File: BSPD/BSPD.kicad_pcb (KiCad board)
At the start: 2 copper layers, 100.3 x 69.5 mm, 81 parts, among them Q1 BC548, Q2 BC548, Q3 BC548, Q4 BC548, Q5 BC548, SW1 SW_DPDT_x2, U1 TL431D, U2 LM358, U3 LM358, U4 ICL7660, U5 LM358, U6 4001

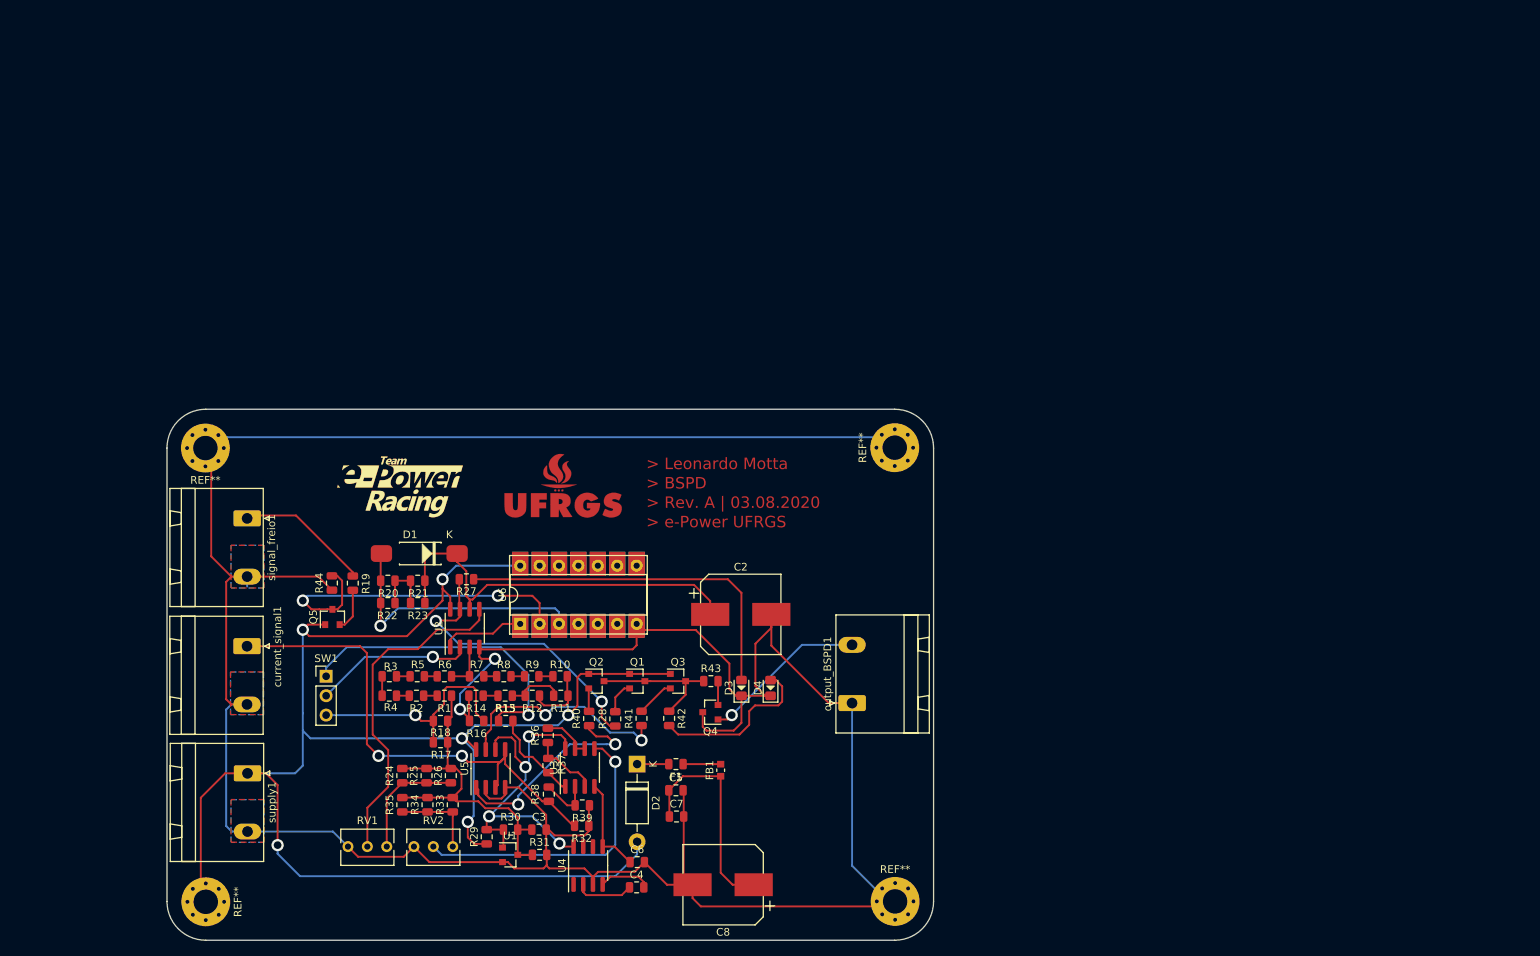
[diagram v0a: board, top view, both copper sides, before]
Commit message: schematic update BSPD and new layout not finishet
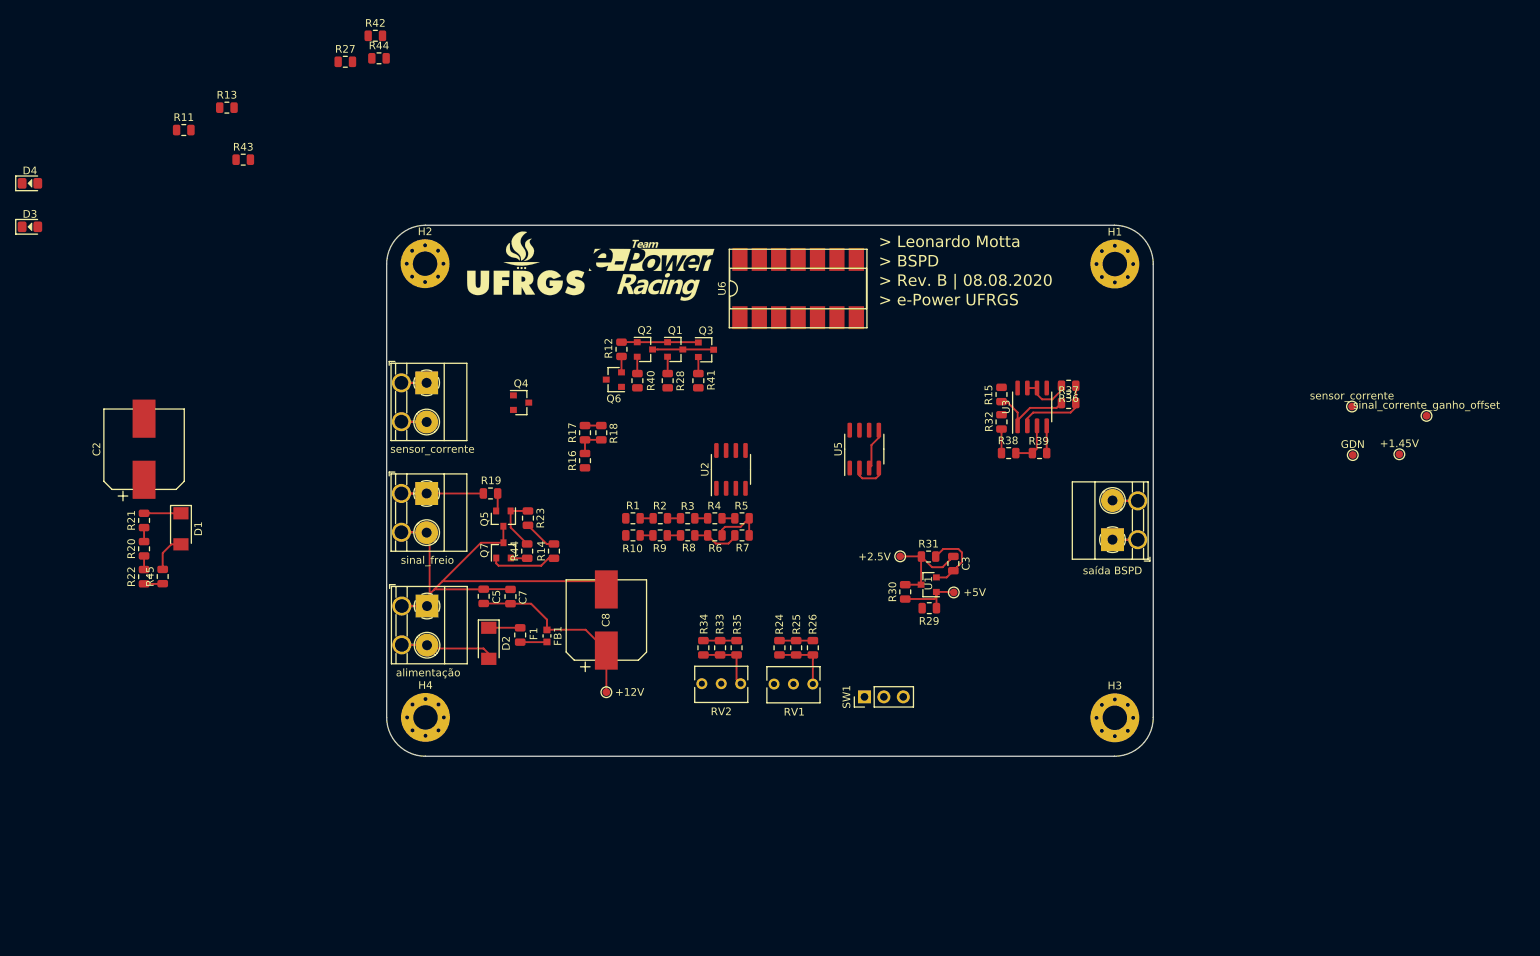
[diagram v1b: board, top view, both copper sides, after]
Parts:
- removed C4: 10uF, Capacitor_SMD:C_0805_2012Metric
- removed C6: 100nF, Capacitor_SMD:C_0805_2012Metric
- removed the R44 at (87.6, 119.4)
- removed REF** (x4): MountingHole_3.2mm_M3_Pad_Via, e-Power:MountingHole_3.2mm_M3_Pad_Via
- removed U4: ICL7660, Package_SO:SOIC-8_3.9x4.9mm_P1.27mm
- removed current_signal1, output_BSPD1, signal_freio1, supply1: Screw_Terminal_01x02, Connector_Phoenix_GMSTB:PhoenixContact_GMSTBA_2,5_2-G-7,62_1x02_P7.62mm_Horizontal
- added H1: MountingHole_Pad, e-Power:MountingHole_3.2mm_M3_Pad_Via, F.Cu at (190.1, 77.6)
- added H2: MountingHole_Pad, e-Power:MountingHole_3.2mm_M3_Pad_Via, F.Cu at (99.8, 77.6)
- added H3: MountingHole_Pad, e-Power:MountingHole_3.2mm_M3_Pad_Via, F.Cu at (190.1, 137.0)
- added H4: MountingHole_Pad, e-Power:MountingHole_3.2mm_M3_Pad_Via, F.Cu at (99.9, 137.0)
- added Q6: BC557, Package_TO_SOT_SMD:SOT-23, F.Cu at (124.5, 92.7)
- added Q7: BC548, Package_TO_SOT_SMD:SOT-23, F.Cu at (110.1, 115.1)
- added R44: 1k, Resistor_SMD:R_0805_2012Metric, F.Cu at (93.8, 50.7)
- added R44: 10k, Resistor_SMD:R_0805_2012Metric, F.Cu at (113.2, 115.2)
- added R45: 10R, Resistor_SMD:R_0805_2012Metric, F.Cu at (65.5, 118.5)
- added TP1: +5V, e-Power:TestPoint_Pad_D1.0mm, F.Cu at (169.0, 120.6)
- added TP2: +1.45V, e-Power:TestPoint_Pad_D1.0mm, F.Cu at (227.3, 102.5)
- added TP3: +2.5V, e-Power:TestPoint_Pad_D1.0mm, F.Cu at (162.0, 115.9)
- added TP4: GDN, e-Power:TestPoint_Pad_D1.0mm, F.Cu at (221.2, 102.6)
- added TP5: sensor_corrente, e-Power:TestPoint_Pad_D1.0mm, F.Cu at (221.1, 96.3)
- added TP6: sinal_corrente_ganho_offset, e-Power:TestPoint_Pad_D1.0mm, F.Cu at (230.9, 97.5)
- added TP7: +12V, e-Power:TestPoint_Pad_D1.0mm, F.Cu at (123.5, 133.7)
- added alimentação: Screw_Terminal_01x02, e-Power:TerminalBlock_Phoenix_MKDS-1,5-2_1x02_P5.08mm_Horizontal, F.Cu at (100.1, 122.4)
- added saída BSPD: Screw_Terminal_01x02, e-Power:TerminalBlock_Phoenix_MKDS-1,5-2_1x02_P5.08mm_Horizontal, F.Cu at (189.8, 113.7)
- added sensor_corrente: Screw_Terminal_01x02, e-Power:TerminalBlock_Phoenix_MKDS-1,5-2_1x02_P5.08mm_Horizontal, F.Cu at (100.0, 93.2)
- added sinal_freio: Screw_Terminal_01x02, e-Power:TerminalBlock_Phoenix_MKDS-1,5-2_1x02_P5.08mm_Horizontal, F.Cu at (100.0, 107.6)
- C2, C8: value 470uF -> 220uF
- D1: value DIODE -> SS54HF; footprint e-Power:DO-41_SMD -> e-Power:DO-214AC
- D2: footprint Diode_THT:D_DO-41_SOD81_P10.16mm_Horizontal -> e-Power:DO-214AC
- G1: footprint e-Power:e-Power_16.5x8.0mm_Copper -> e-Power:Logo_e-Power_16.5x8.0mm_SilkS
- G2: footprint e-Power:UFRGS_14.7x8.0mm_Copper -> e-Power:Logo_UFRGS_14.7x8.0mm_SilkS
- R11, R23: value 10k -> 1k
- moved D4 117.3 mm to (48.1, 67.1), turned to 0 degrees
- moved D3 111.0 mm to (48.1, 72.7), turned to 0 degrees
- moved R42 97.3 mm to (93.3, 47.7), turned to 0 degrees
- moved R43 91.7 mm to (76.0, 64.0)
- moved R11 89.0 mm to (68.2, 60.1), turned to 0 degrees
- moved R13 85.1 mm to (73.9, 57.1), turned to 0 degrees
- moved R37 83.0 mm to (184.0, 95.8), turned to 0 degrees
- moved R36 82.1 mm to (184.0, 93.5), turned to 180 degrees
- moved C2 81.0 mm to (63.0, 101.9), turned to 90 degrees
- moved R15 77.7 mm to (175.3, 94.7), turned to 270 degrees
- moved R32 76.2 mm to (175.3, 98.3), turned to 270 degrees
- moved U3 75.7 mm to (179.3, 96.3)
- moved R39 75.5 mm to (180.2, 102.4)
- moved R38 74.9 mm to (176.2, 102.4), turned to 180 degrees
- moved SW1 70.5 mm to (157.3, 134.3), turned to 90 degrees
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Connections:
- C3 pad 1: Vref -> VREF
- D2 pad 2: +12V -> Input_Power
- Q1 pad 1: +12V -> Net-(Q1-Pad1)
- Q1 pad 3: Net-(Q1-Pad3) -> GNDREF
- Q2 pad 1: +12V -> Net-(Q1-Pad1)
- Q2 pad 3: Net-(Q1-Pad3) -> GNDREF
- Q3 pad 1: +12V -> Net-(Q1-Pad1)
- Q3 pad 3: Net-(Q1-Pad3) -> GNDREF
- Q5 pad 1: +12V -> Net-(Q5-Pad1)
- Q5 pad 3: Net-(Q5-Pad3) -> GNDREF
- R1 pad 1: Vref -> VREF
- R10 pad 1: Net-(R10-Pad1) -> GNDREF
- R11 pad 1: Net-(R10-Pad1) -> +12V
- R11 pad 2: Net-(R11-Pad2) -> Net-(Q1-Pad1)
- R12 pad 1: Net-(R10-Pad1) -> Net-(Q1-Pad1)
- R12 pad 2: Net-(R11-Pad2) -> Net-(Q6-Pad2)
- R13 pad 1: Net-(R11-Pad2) -> Net-(Q6-Pad1)
- R14 pad 1: Net-(R13-Pad2) -> Net-(Q7-Pad1)
- R14 pad 2: GNDREF -> +12V
- R17 pad 2: Vref -> VREF
- R18 pad 2: Vref -> VREF
- R2 pad 1: Net-(R1-Pad2) -> Net-(R2-Pad1)
- R2 pad 2: Net-(R2-Pad2) -> Net-(R1-Pad2)
- R20 pad 1: Net-(D1-Pad2) -> Net-(R20-Pad1)
- R22 pad 1: Net-(D1-Pad2) -> Net-(R22-Pad1)
- R22 pad 2: Net-(R20-Pad2) -> Net-(R20-Pad1)
- R23 pad 1: Net-(R20-Pad2) -> Net-(Q5-Pad1)
- R23 pad 2: Net-(C2-Pad1) -> +12V
- R24 pad 2: Vref -> 5V
- R25 pad 2: Vref -> 5V
- R26 pad 2: Vref -> 5V
- R3 pad 2: Net-(R2-Pad2) -> Net-(R2-Pad1)
- R30 pad 2: Vref -> VREF
- R31 pad 1: Vref -> VREF
- R32 pad 2: current_out -> Net-(R32-Pad2)
- R33 pad 2: Vref -> VREF
- R34 pad 2: Vref -> VREF
- R35 pad 2: Vref -> VREF
- R38 pad 2: current_out -> Net-(R32-Pad2)
- R42 pad 1: Net-(Q1-Pad3) -> Net-(Q6-Pad1)
- R43 pad 1: Net-(Q1-Pad3) -> Net-(R13-Pad2)
- R7 pad 1: Net-(R7-Pad1) -> Net-(R6-Pad1)
- R7 pad 2: Net-(R6-Pad1) -> Net-(R5-Pad1)
- R8 pad 2: Net-(R7-Pad1) -> Net-(R6-Pad1)
- U1 pad 3: Vref -> VREF
- U2 pad 3: Net-(R6-Pad1) -> Net-(R4-Pad1)
- U3 pad 2: Net-(R38-Pad1) -> Net-(R36-Pad1)
- U3 pad 3: Net-(R36-Pad1) -> Net-(R38-Pad1)
- U3 pad 4: -5V -> GNDREF
- U6 pad 2: Net-(Q5-Pad3) -> Net-(Q7-Pad1)
- U6 pad 3: Net-(D1-Pad2) -> Net-(R22-Pad1)
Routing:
- net GNDREF: track 436.0 -> 82.7 mm, vias 2 -> 0
- net +12V: track 254.1 -> 29.3 mm, vias 6 -> 0
- net current_out: track 68.0 -> 5.48 mm, vias 2 -> 0
- net Net-(C2-Pad1): track 54.0 -> 4.83 mm
- net Net-(D3-Pad2): track 47.2 -> 0.00 mm
- net Vref: track 46.6 -> 0.00 mm
- net Net-(Q5-Pad3): track 45.0 -> 0.00 mm, vias 2 -> 0
- net Net-(RV1-Pad2): track 43.6 -> 0.00 mm
- net Net-(R15-Pad1): track 40.4 -> 0.00 mm, vias 1 -> 0
- net Net-(RV2-Pad2): track 39.1 -> 0.00 mm, vias 1 -> 0
- net Net-(R27-Pad1): track 38.8 -> 0.00 mm, vias 2 -> 0
- net 5V: track 46.1 -> 13.7 mm, vias 4 -> 0
- net Net-(D1-Pad2): track 35.6 -> 5.00 mm, vias 1 -> 0
- net Net-(R41-Pad1): track 29.7 -> 0.00 mm, vias 2 -> 0
- net Net-(R40-Pad1): track 28.2 -> 0.00 mm, vias 2 -> 0
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- removed copper zone on B.Cu, net GNDREF
- removed copper zone on F.Cu, net GNDREF
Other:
- net class Default: clearance 0.127 -> 0.2; trace_width 0.254 -> 0.25; via_dia 1.6 -> 0.8; via_drill 1 -> 0.4
- rule trace_clearance: 0.127 -> 0.2
- board text added: "> Rev. B | 08.08.2020"
- board text removed: "> Rev. A | 03.08.2020"

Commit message: Rev. B - BSPD and Rev. B - Set/Reset
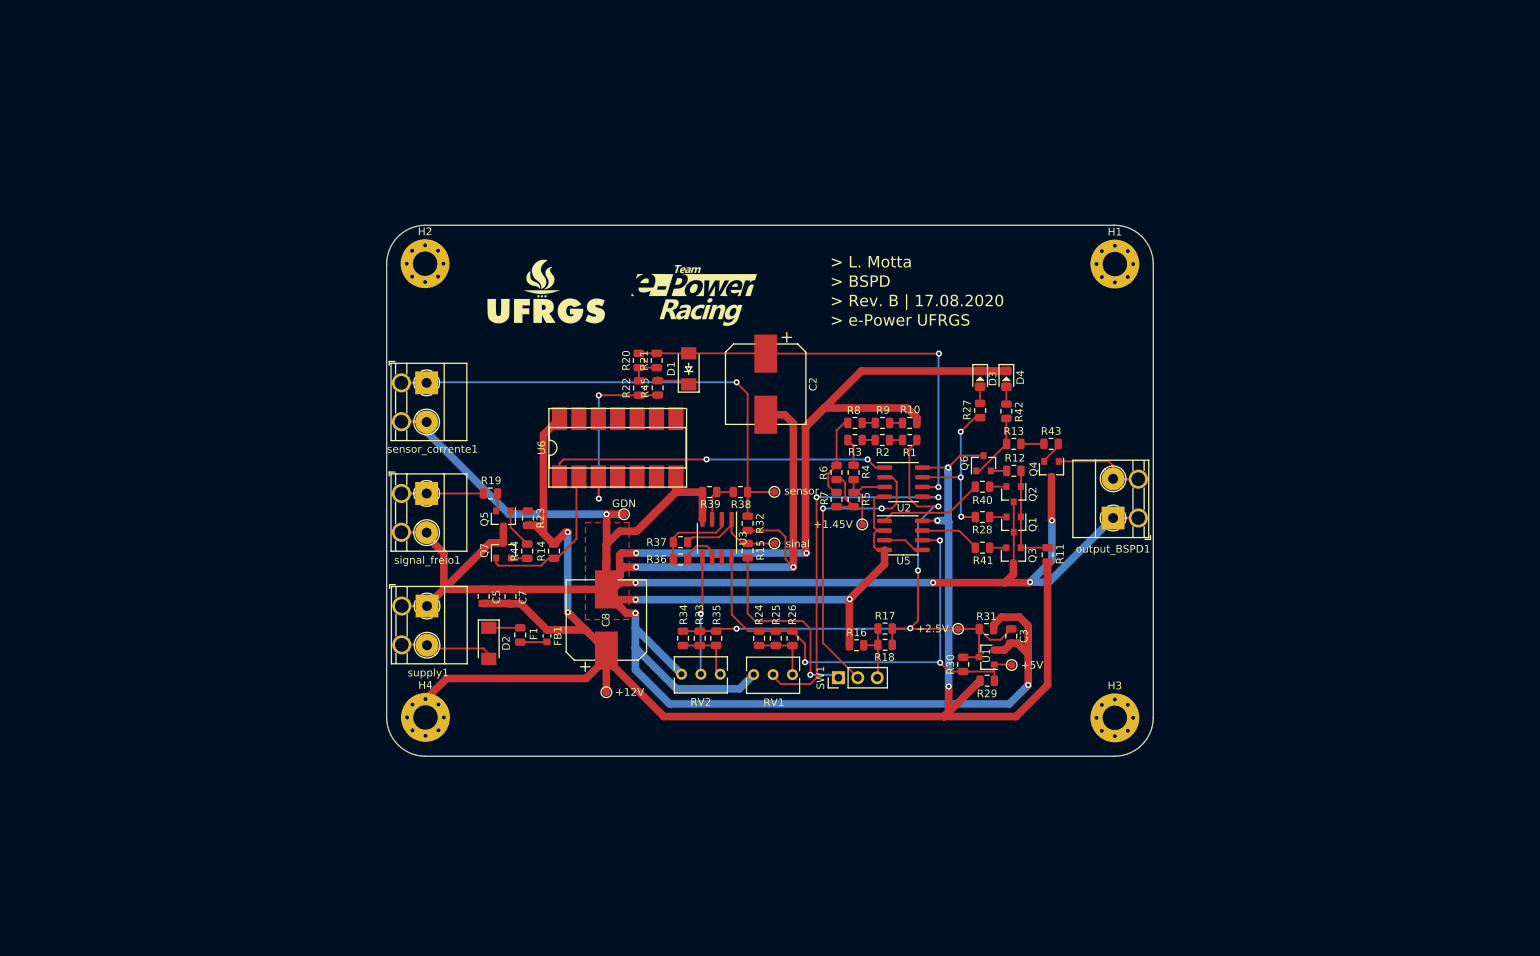
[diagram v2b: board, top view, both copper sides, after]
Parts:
- removed the R44 at (93.8, 50.7)
- removed saída BSPD: Screw_Terminal_01x02, e-Power:TerminalBlock_Phoenix_MKDS-1,5-2_1x02_P5.08mm_Horizontal
- added output_BSPD1: Screw_Terminal_01x02, e-Power:TerminalBlock_Phoenix_MKDS-1,5-2_1x02_P5.08mm_Horizontal, F.Cu at (189.9, 110.9)
- D1: value SS54HF -> 1N5819
- G1: value e-Power_16.5x8.0mm_Copper -> Logo_UFRGS_Large; footprint e-Power:Logo_e-Power_16.5x8.0mm_SilkS -> e-Power:Logo_UFRGS_14.7x8.0mm_SilkS
- G2: value UFRGS_1_14.7x8.0mm_Copper -> Logo_e-Power_Large; footprint e-Power:Logo_UFRGS_14.7x8.0mm_SilkS -> e-Power:Logo_e-Power_16.5x8.0mm_SilkS
- R20: value 1k -> 10k
- TP5: value sensor_corrente -> sensor
- TP6: value sinal_corrente_ganho_offset -> sinal
- moved D4 130.3 mm to (175.9, 92.6), turned to 270 degrees
- moved R11 126.0 mm to (181.3, 115.7), turned to 90 degrees
- moved D3 125.9 mm to (172.5, 92.6), turned to 270 degrees
- moved R43 112.1 mm to (181.8, 101.2)
- moved R13 112.0 mm to (176.9, 101.2)
- moved R42 96.1 mm to (175.9, 96.9), turned to 90 degrees
- moved TP4 95.7 mm to (125.9, 110.4)
- moved R27 94.8 mm to (172.5, 96.8), turned to 90 degrees
- moved TP6 87.0 mm to (145.5, 114.2)
- moved C2 81.8 mm to (144.4, 93.3), turned to 270 degrees
- moved TP5 76.4 mm to (145.5, 107.4)
- moved TP2 70.9 mm to (157.0, 111.7)
- moved R21 70.3 mm to (130.1, 90.2)
- moved Q4 70.0 mm to (181.8, 104.4), turned to 270 degrees
- moved D1 69.7 mm to (134.3, 91.3), turned to 90 degrees
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- renumbered sensor_corrente to sensor_corrente1, sinal_freio to signal_freio1, alimentação to supply1
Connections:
- D1 pad 1: Net-(C2-Pad1) -> Net-(D1-Pad1)
- D1 pad 2: Net-(D1-Pad2) -> Net-(C2-Pad1)
- R20 pad 2: Net-(R20-Pad2) -> Net-(C2-Pad1)
- R21 pad 1: Net-(R20-Pad2) -> Net-(R20-Pad1)
- R45 pad 2: Net-(D1-Pad2) -> Net-(D1-Pad1)
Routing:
- net GNDREF: track 82.7 -> 538.6 mm, vias 0 -> 13
- net +12V: track 29.3 -> 223.3 mm, vias 0 -> 5
- net VREF: track 20.5 -> 84.9 mm, vias 0 -> 4
- net Net-(R32-Pad2): track 3.15 -> 62.0 mm, vias 0 -> 1
- net 5V: track 13.7 -> 69.9 mm, vias 0 -> 3
- net Net-(C2-Pad1): track 4.83 -> 58.9 mm, vias 0 -> 2
- net Net-(RV1-Pad2): track 0.00 -> 48.4 mm, vias 0 -> 2
- net Net-(U2-Pad1): track 0.00 -> 45.0 mm, vias 0 -> 2
- net Net-(SW1-Pad2): track 0.00 -> 38.6 mm, vias 0 -> 2
- net Net-(R15-Pad1): track 0.00 -> 26.2 mm, vias 0 -> 1
- net Net-(R22-Pad1): track 2.45 -> 24.1 mm, vias 0 -> 2
- net Net-(R27-Pad1): track 0.00 -> 21.3 mm, vias 0 -> 3
- net Net-(RV2-Pad2): track 0.00 -> 15.5 mm, vias 0 -> 1
- net Net-(R40-Pad1): track 0.00 -> 13.7 mm
- net Net-(Q7-Pad1): track 8.78 -> 21.0 mm
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- added copper zone on F.Cu, net GNDREF
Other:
- board text added: "> L. Motta"
- board text added: "> Rev. B | 17.08.2020"
- board text removed: "> Leonardo Motta"
- board text removed: "> Rev. B | 08.08.2020"

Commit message: BSPD att.
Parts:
- added TP10: CAPACITOR, e-Power:TestPoint_Pad_D1.0mm, F.Cu at (165.3, 85.9)
- added TP11: ERRO_BSPD, e-Power:TestPoint_Pad_D1.0mm, F.Cu at (167.8, 85.9)
- added TP12: SHORT_SENSOR, e-Power:TestPoint_Pad_D1.0mm, F.Cu at (177.3, 85.9)
- added TP13: SENSOR_OPEN, e-Power:TestPoint_Pad_D1.0mm, F.Cu at (174.9, 85.9)
- added TP14: ERRO_GERAL, e-Power:TestPoint_Pad_D1.0mm, F.Cu at (170.1, 85.9)
- added TP15: GDN, e-Power:TestPoint_Pad_D1.0mm, F.Cu at (172.5, 85.8)
- added TP8: COMP_OUT, e-Power:TestPoint_Pad_D1.0mm, F.Cu at (162.9, 85.8)
- added TP9: FREIO_SINAL, e-Power:TestPoint_Pad_D1.0mm, F.Cu at (160.6, 85.8)
- TP5: value sensor -> sensor_corrente
- TP6: value sinal -> sinal_corrente_ganho_offset
- moved TP1 51.6 mm to (125.6, 138.0)
- moved TP3 48.3 mm to (123.0, 138.0), turned to 180 degrees
- moved TP4 28.7 mm to (117.9, 137.9)
- moved G2 22.9 mm to (113.9, 90.6)
- moved output_BSPD1 7.83 mm to (189.8, 118.7)
- moved TP7 5.27 mm to (120.5, 137.9)
- moved G1 3.84 mm to (114.1, 77.7)
- moved supply1 0.43 mm to (100.1, 122.8)
- moved sensor_corrente1 0.18 mm to (100.1, 93.0)
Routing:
- net VREF: track 84.9 -> 174.9 mm, vias 4 -> 6
- net 5V: track 69.9 -> 139.1 mm, vias 3 -> 5
- net Net-(Q7-Pad1): track 21.0 -> 79.0 mm, vias 0 -> 2
- net GNDREF: track 538.6 -> 579.0 mm, vias 13 -> 15
- net current_comp2: track 2.16 -> 37.9 mm, vias 0 -> 2
- net current_comp: track 2.21 -> 24.3 mm
- net Net-(TP8-Pad1): track 45.0 -> 66.3 mm, vias 2 -> 3
- net Net-(Q6-Pad1): track 8.77 -> 28.5 mm, vias 0 -> 2
- net Net-(R27-Pad1): track 21.3 -> 36.7 mm, vias 3 -> 4
- net Net-(Q4-Pad1): track 8.64 -> 16.3 mm
- net +12V: track 223.3 -> 229.6 mm
- net Input_Power: track 9.02 -> 12.6 mm
- net Net-(R32-Pad2): track 62.0 -> 65.4 mm
- net Net-(R19-Pad2): track 7.34 -> 10.7 mm
- net Net-(C2-Pad1): track 58.9 -> 61.3 mm

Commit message: Set/Reset Rev. C
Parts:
- TP12: value SHORT_SENSOR -> SENSOR_CURTO
- TP13: value SENSOR_OPEN -> SENSOR_ABERTO
- TP5: value sensor_corrente -> CORRENTE_IN
- TP6: value sinal_corrente_ganho_offset -> CORRENTE_OUT
- moved TP5 37.0 mm to (124.9, 138.1), turned to 90 degrees
- moved TP6 29.8 mm to (124.9, 135.7)
- moved TP4 4.03 mm to (113.9, 137.9)
- moved TP7 3.98 mm to (116.5, 137.9)
- moved TP3 3.77 mm to (119.2, 138.0)
- moved TP1 3.68 mm to (121.9, 138.0)
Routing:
- net Net-(R32-Pad2): track 65.4 -> 113.1 mm, vias 1 -> 3
- net Signal: track 15.4 -> 56.2 mm, vias 0 -> 2
- net 5V: track 139.1 -> 144.7 mm
- net VREF: track 174.9 -> 180.2 mm
- net GNDREF: track 579.0 -> 580.6 mm
- net +12V: track 229.6 -> 230.7 mm
